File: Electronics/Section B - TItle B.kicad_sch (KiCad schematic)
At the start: 30 parts, among them J10 Conn_01x02, J11 JST_SHBM04B-SRSS-TB, J12 JST_SHBM04B-SRSS-TB, J3 RJ45_RB1-125B8G1A, J4 Conn_01x07, J5 Micro_SD_Card_Det, J6 Conn_01x04, J7 Conn_02x07_Odd_Even, J8 JST_SHBM04B-SRSS-TB, J9 JST_SHBM04B-SRSS-TB, Q1 PMOS, U2 TPD4EUSB30, U3 TPD4EUSB30, U4 74LVC1G07SE-7, U5 RT9742GGJ5

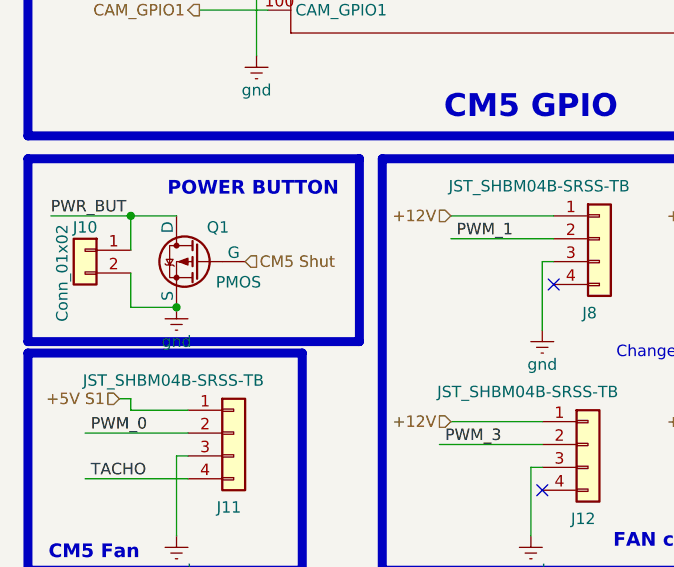
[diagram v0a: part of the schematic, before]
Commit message: More pcb arangment, verticle ports
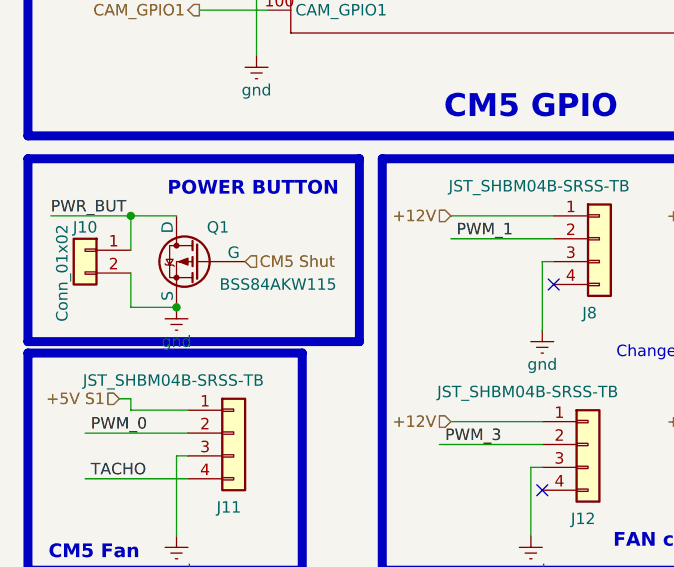
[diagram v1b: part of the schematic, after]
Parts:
- Q1: value PMOS -> BSS84AKW115
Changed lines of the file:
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@@
 		(polyline
 			(pts
-				(xy 306.07 137.16) (xy 308.61 137.16) (xy 308.61 142.24) (xy 306.07 142.24)
+				(xy 306.07 110.49) (xy 306.07 123.19) (xy 308.61 123.19) (xy 308.61 110.49)
 			)
 			(stroke
@@
 		(polyline
 			(pts
-				(xy 306.07 110.49) (xy 306.07 123.19) (xy 308.61 123.19) (xy 308.61 110.49)
+				(xy 267.97 48.26) (xy 275.59 48.26) (xy 276.86 49.53) (xy 276.86 80.01) (xy 267.97 80.01)
 			)
 			(stroke
@@
 		(polyline
 			(pts
-				(xy 267.97 48.26) (xy 275.59 48.26) (xy 276.86 49.53) (xy 276.86 80.01) (xy 267.97 80.01)
+				(xy 306.07 137.16) (xy 308.61 137.16) (xy 308.61 142.24) (xy 306.07 142.24)
 			)
 			(stroke
@@
 			)
 		)
-		(property "Value" "PMOS"
-			(at 39.878 183.896 0)
+		(property "Value" "BSS84AKW115"
+			(at 48.26 184.15 0)
 			(effects
 				(font
